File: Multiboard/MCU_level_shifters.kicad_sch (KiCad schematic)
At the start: 45 parts, among them Q1 Q_Dual_NMOS_G1S2G2D2S1D1, Q14 Q_Dual_NMOS_G1S2G2D2S1D1, Q2 Q_Dual_NMOS_G1S2G2D2S1D1, Q3 Q_Dual_NMOS_G1S2G2D2S1D1, Q4 Q_Dual_NMOS_G1S2G2D2S1D1, Q5 Q_Dual_NMOS_G1S2G2D2S1D1, Q6 Q_Dual_NMOS_G1S2G2D2S1D1, Q7 Q_Dual_NMOS_G1S2G2D2S1D1, SW3 SW_SPST, SW4 SW_SPST, SW5 SW_SPST, SW7 SW_SPST, SW9 SW_SPST

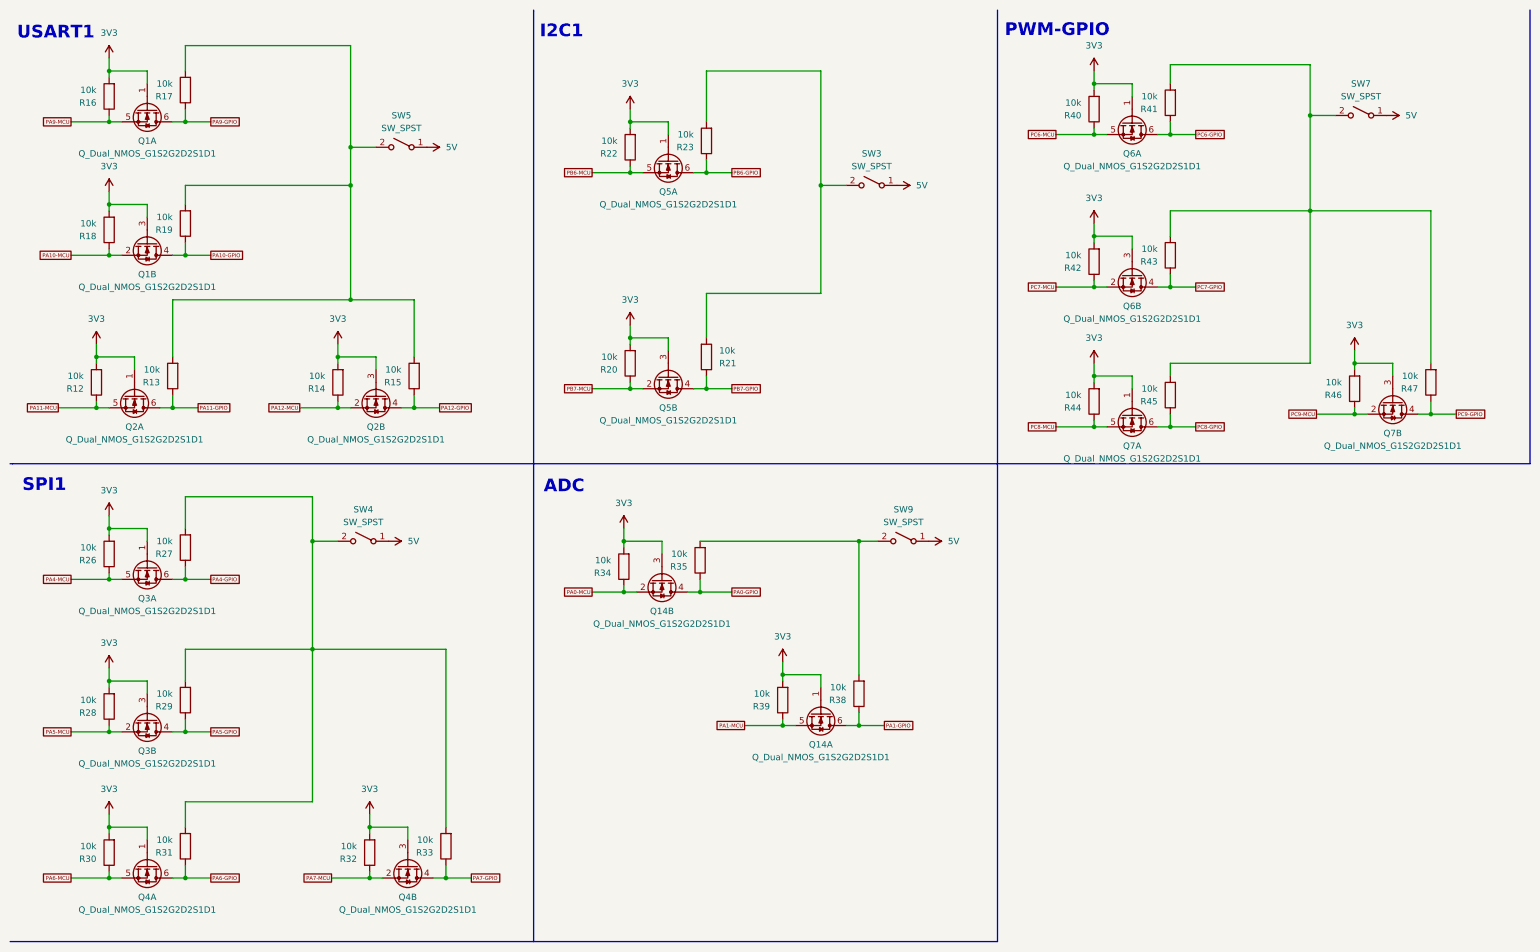
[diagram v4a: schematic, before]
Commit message: wired level shifters; positioed ldo and charge pump
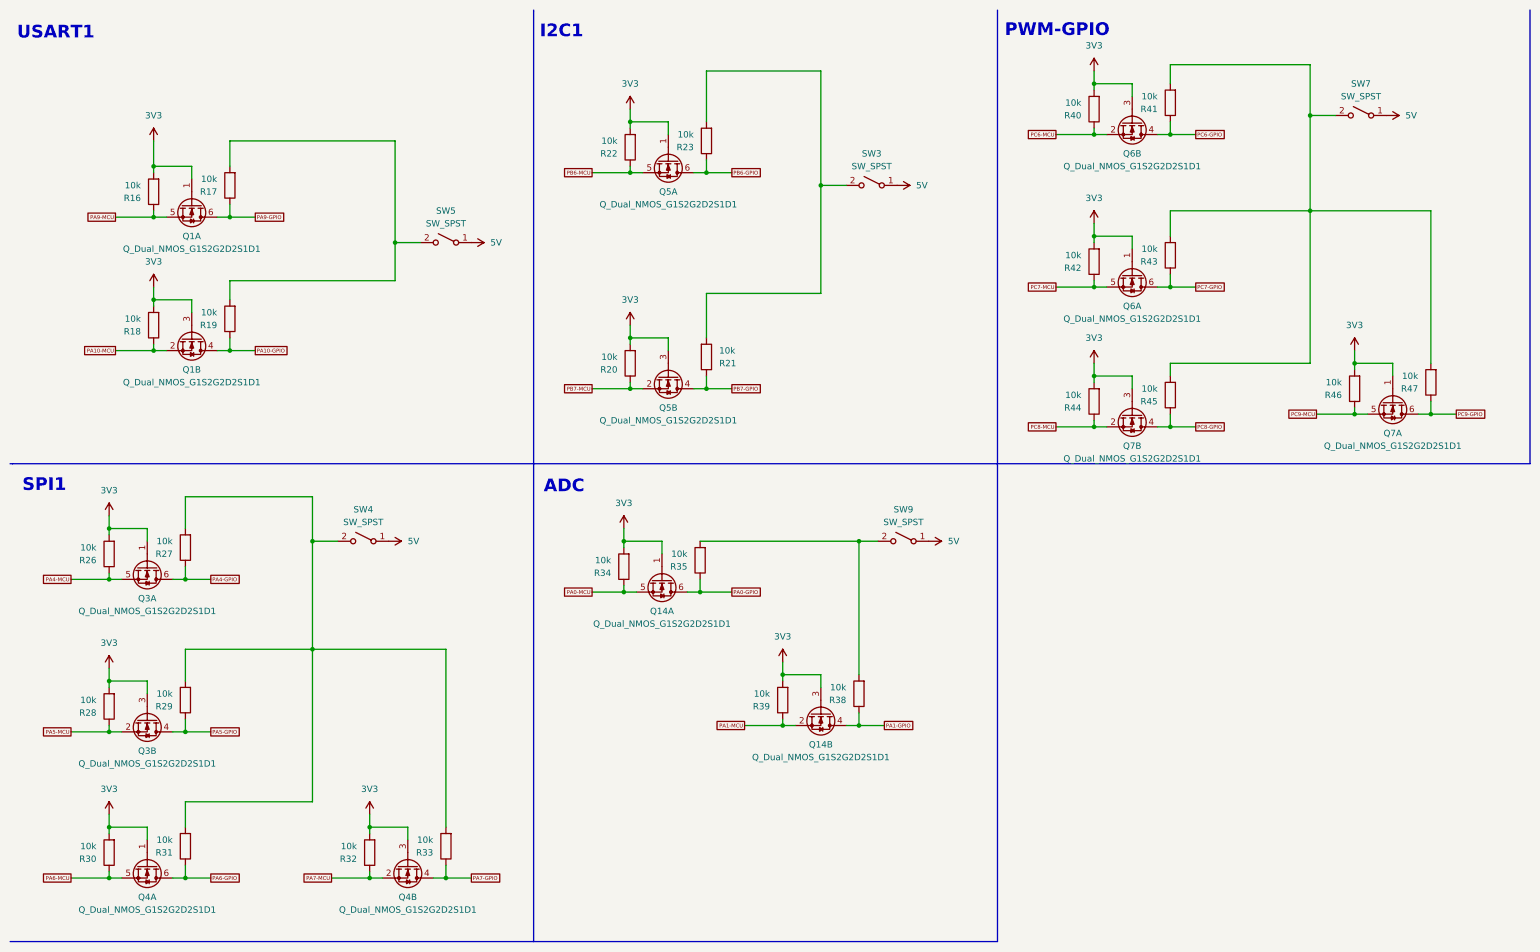
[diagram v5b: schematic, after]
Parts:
- removed Q2: Q_Dual_NMOS_G1S2G2D2S1D1, Package_TO_SOT_SMD:SOT-23-6_Handsoldering, symbol Transistor_FET:Q_Dual_NMOS_G1S2G2D2S1D1
- removed R12, R13, R14, R15: 10k, Resistor_SMD:R_0603_1608Metric_Pad0.98x0.95mm_HandSolder, symbol Device:R
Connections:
- net 3V3: now also Q14.1 (G), Q14.3 (G), Q6.1 (G), Q6.3 (G), Q7.1 (G), Q7.3 (G); no longer Q14.1 (G), Q14.3 (G), Q6.1 (G), Q6.3 (G), Q7.1 (G), Q7.3 (G)
- net PA0-GPIO: now also Q14.6 (D); no longer Q14.4 (D)
- net PA0-MCU: now also Q14.5 (S); no longer Q14.2 (S)
- net PA1-GPIO: now also Q14.4 (D); no longer Q14.6 (D)
- net PA1-MCU: now also Q14.2 (S); no longer Q14.5 (S)
- net PC6-GPIO: now also Q6.4 (D); no longer Q6.6 (D)
- net PC6-MCU: now also Q6.2 (S); no longer Q6.5 (S)
- net PC7-GPIO: now also Q6.6 (D); no longer Q6.4 (D)
- net PC7-MCU: now also Q6.5 (S); no longer Q6.2 (S)
- net PC8-GPIO: now also Q7.4 (D); no longer Q7.6 (D)
- net PC8-MCU: now also Q7.2 (S); no longer Q7.5 (S)
- net PC9-GPIO: now also Q7.6 (D); no longer Q7.4 (D)
- net PC9-MCU: now also Q7.5 (S); no longer Q7.2 (S)
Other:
- moved on the sheet: Q1A, Q1B, R16, R17, R18, R19, SW5

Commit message: Wired usb
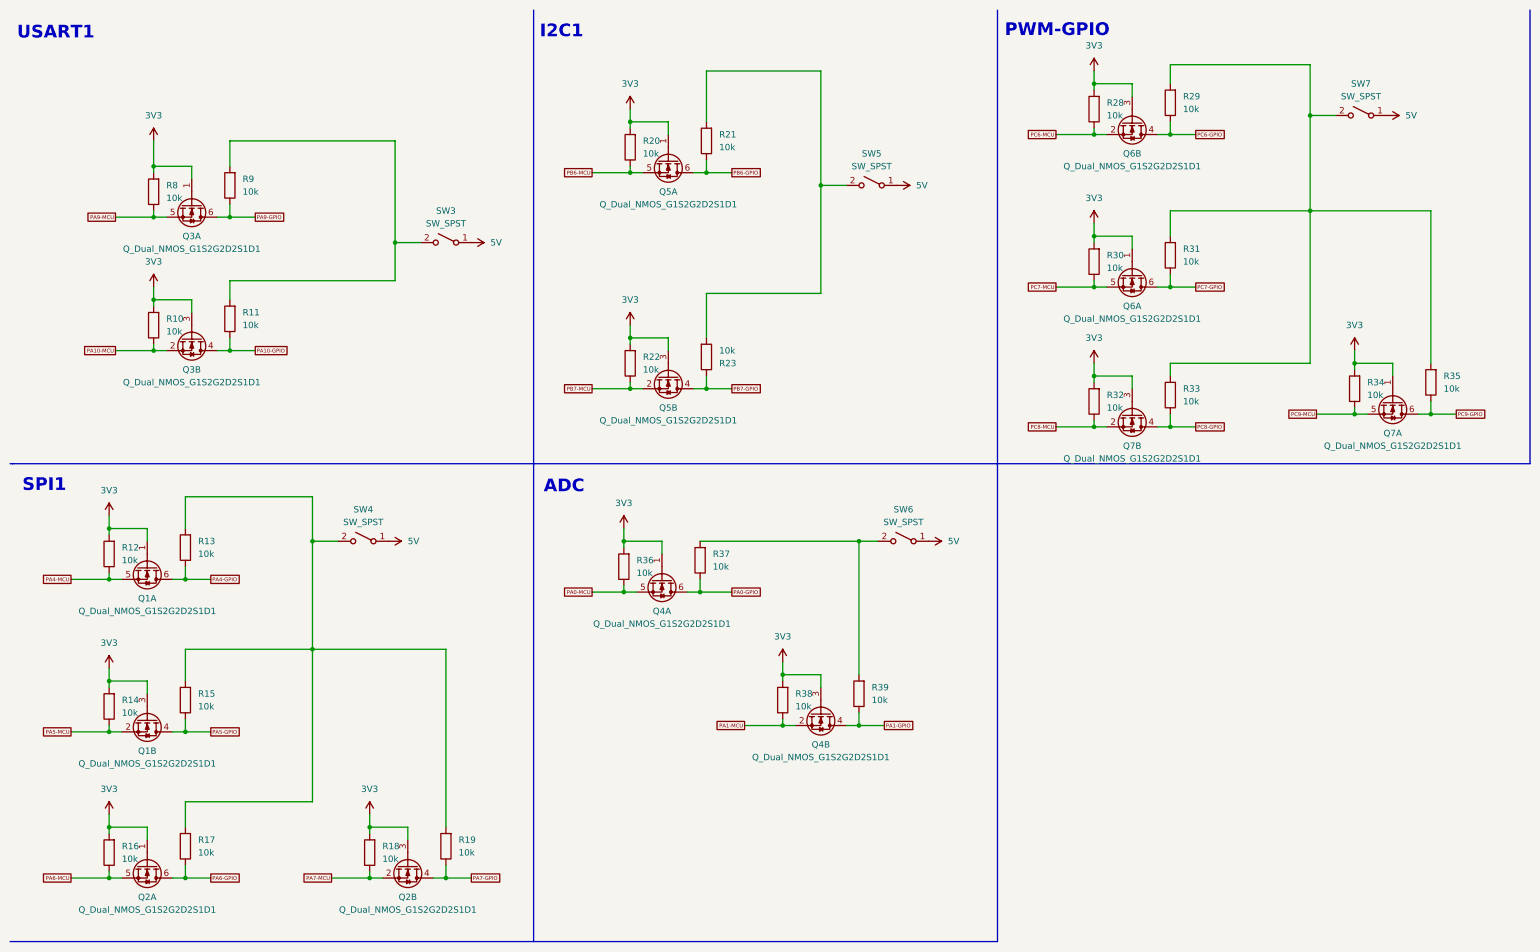
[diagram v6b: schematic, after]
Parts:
- renumbered Q3 to Q1, Q4 to Q2, Q1 to Q3, Q14 to Q4, R18 to R10, R19 to R11, R26 to R12, R27 to R13, R28 to R14, R29 to R15, R30 to R16, R31 to R17, R32 to R18, R33 to R19, R22 to R20, R23 to R21, R20 to R22, R21 to R23, R40 to R28, R41 to R29, R42 to R30, R43 to R31, R44 to R32, R45 to R33, R46 to R34, R47 to R35, R34 to R36, R35 to R37, R39 to R38, R38 to R39, R16 to R8, R17 to R9, SW5 to SW3, SW3 to SW5, SW9 to SW6

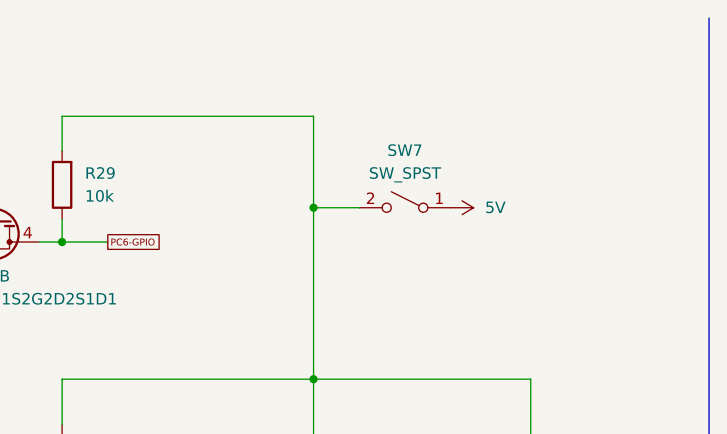
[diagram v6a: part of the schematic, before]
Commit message: Completed mcu usb-c, mcu oscillators and mcu jtag pins
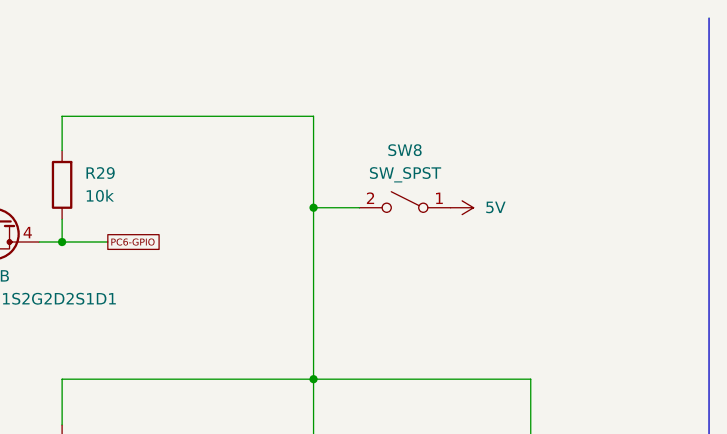
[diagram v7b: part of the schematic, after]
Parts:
- renumbered SW7 to SW8
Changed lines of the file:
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@@
 		(dnp no)
 		(fields_autoplaced yes)
-		(property "Reference" "SW7"
+		(property "Reference" "SW8"
 			(at 281.94 26.67 0)
 			(effects
@@
 			(project "Multiboard"
 				(path "/9ed4a389-3aa7-41f1-b239-280eb7f09ef1/2bca3eb5-73b3-4aa8-9f30-e1743a374253/218b9c79-34c6-4f16-af2d-c91825215b5a"
-					(reference "SW7")
+					(reference "SW8")
 					(unit 1)
 				)

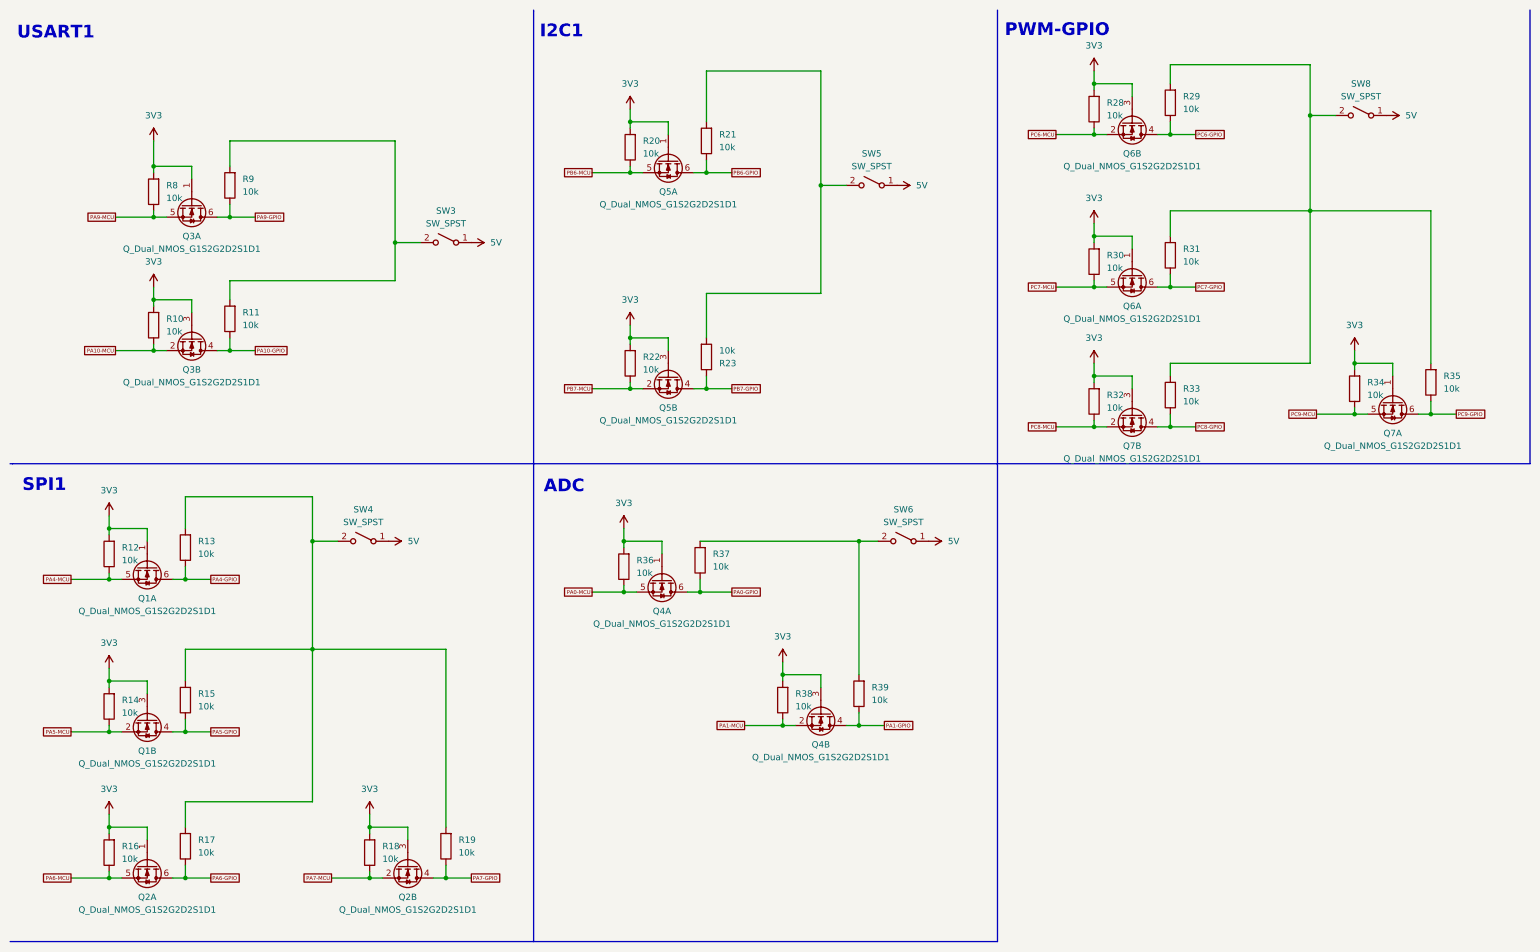
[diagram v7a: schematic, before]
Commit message: synchronised sch and pcb. Added jtag connection between fpga and ftdi
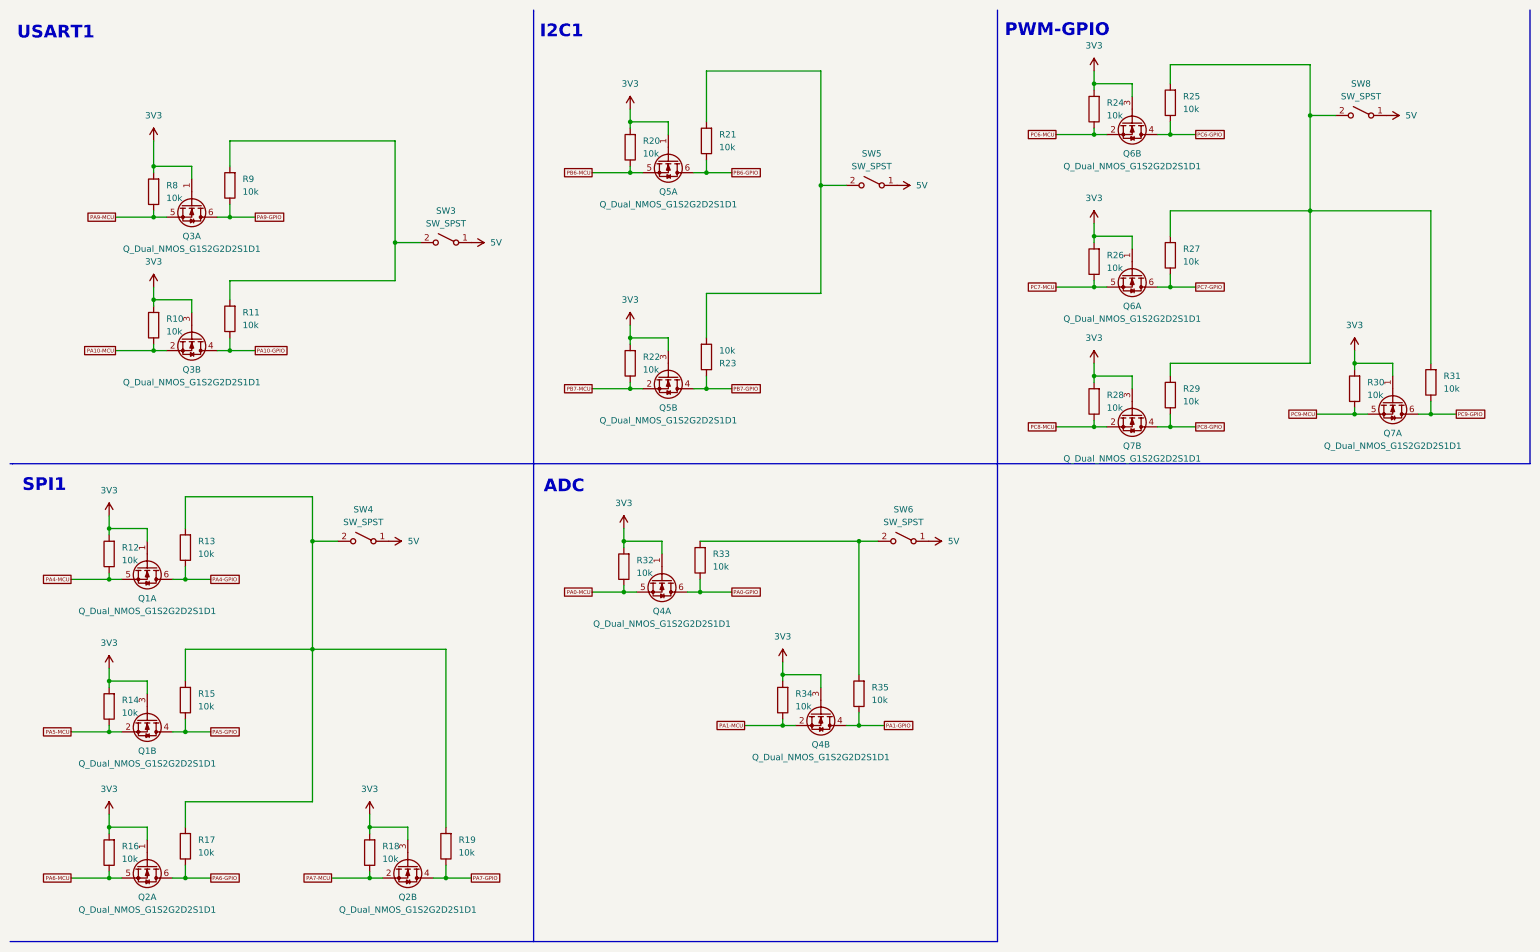
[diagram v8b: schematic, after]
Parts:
- renumbered R28 to R24, R29 to R25, R30 to R26, R31 to R27, R32 to R28, R33 to R29, R34 to R30, R35 to R31, R36 to R32, R37 to R33, R38 to R34, R39 to R35
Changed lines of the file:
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@@
 		(dnp no)
 		(fields_autoplaced yes)
-		(property "Reference" "R36"
+		(property "Reference" "R32"
 			(at 137.16 121.9199 0)
 			(effects
@@
 			(project "Multiboard"
 				(path "/9ed4a389-3aa7-41f1-b239-280eb7f09ef1/2bca3eb5-73b3-4aa8-9f30-e1743a374253/218b9c79-34c6-4f16-af2d-c91825215b5a"
-					(reference "R36")
+					(reference "R32")
 					(unit 1)
 				)
@@
 		(dnp no)
 		(fields_autoplaced yes)
-		(property "Reference" "R30"
+		(property "Reference" "R26"
 			(at 231.14 60.9599 0)
 			(effects
@@
 			(project "Multiboard"
 				(path "/9ed4a389-3aa7-41f1-b239-280eb7f09ef1/2bca3eb5-73b3-4aa8-9f30-e1743a374253/218b9c79-34c6-4f16-af2d-c91825215b5a"
-					(reference "R30")
+					(reference "R26")
 					(unit 1)
 				)
@@
 		(dnp no)
 		(fields_autoplaced yes)
-		(property "Reference" "R35"
+		(property "Reference" "R31"
 			(at 298.45 85.0899 0)
 			(effects
@@
 			(project "Multiboard"
 				(path "/9ed4a389-3aa7-41f1-b239-280eb7f09ef1/2bca3eb5-73b3-4aa8-9f30-e1743a374253/218b9c79-34c6-4f16-af2d-c91825215b5a"
-					(reference "R35")
+					(reference "R31")
 					(unit 1)
 				)
@@
 		(dnp no)
 		(fields_autoplaced yes)
-		(property "Reference" "R38"
+		(property "Reference" "R34"
 			(at 168.91 148.5899 0)
 			(effects
@@
 			(project "Multiboard"
 				(path "/9ed4a389-3aa7-41f1-b239-280eb7f09ef1/2bca3eb5-73b3-4aa8-9f30-e1743a374253/218b9c79-34c6-4f16-af2d-c91825215b5a"
-					(reference "R38")
+					(reference "R34")
 					(unit 1)
 				)
@@
 		(dnp no)
 		(fields_autoplaced yes)
-		(property "Reference" "R33"
+		(property "Reference" "R29"
 			(at 246.38 87.6299 0)
 			(effects
@@
 			(project "Multiboard"
 				(path "/9ed4a389-3aa7-41f1-b239-280eb7f09ef1/2bca3eb5-73b3-4aa8-9f30-e1743a374253/218b9c79-34c6-4f16-af2d-c91825215b5a"
-					(reference "R33")
+					(reference "R29")
 					(unit 1)
 				)
@@
 		(dnp no)
 		(fields_autoplaced yes)
-		(property "Reference" "R32"
+		(property "Reference" "R28"
 			(at 231.14 88.8999 0)
 			(effects
@@
 			(project "Multiboard"
 				(path "/9ed4a389-3aa7-41f1-b239-280eb7f09ef1/2bca3eb5-73b3-4aa8-9f30-e1743a374253/218b9c79-34c6-4f16-af2d-c91825215b5a"
-					(reference "R32")
+					(reference "R28")
 					(unit 1)
 				)
@@
 		(dnp no)
 		(fields_autoplaced yes)
-		(property "Reference" "R29"
+		(property "Reference" "R25"
 			(at 246.38 29.2099 0)
 			(effects
@@
 			(project "Multiboard"
 				(path "/9ed4a389-3aa7-41f1-b239-280eb7f09ef1/2bca3eb5-73b3-4aa8-9f30-e1743a374253/218b9c79-34c6-4f16-af2d-c91825215b5a"
-					(reference "R29")
+					(reference "R25")
 					(unit 1)
 				)
@@
 		(dnp no)
 		(fields_autoplaced yes)
-		(property "Reference" "R37"
+		(property "Reference" "R33"
 			(at 152.4 120.6499 0)
 			(effects
@@
 			(project "Multiboard"
 				(path "/9ed4a389-3aa7-41f1-b239-280eb7f09ef1/2bca3eb5-73b3-4aa8-9f30-e1743a374253/218b9c79-34c6-4f16-af2d-c91825215b5a"
-					(reference "R37")
+					(reference "R33")
 					(unit 1)
 				)
@@
 		(dnp no)
 		(fields_autoplaced yes)
-		(property "Reference" "R39"
+		(property "Reference" "R35"
 			(at 184.15 147.3199 0)
 			(effects
@@
 			(project "Multiboard"
 				(path "/9ed4a389-3aa7-41f1-b239-280eb7f09ef1/2bca3eb5-73b3-4aa8-9f30-e1743a374253/218b9c79-34c6-4f16-af2d-c91825215b5a"
-					(reference "R39")
+					(reference "R35")
 					(unit 1)
 				)
@@
 		(dnp no)
 		(fields_autoplaced yes)
-		(property "Reference" "R31"
+		(property "Reference" "R27"
 			(at 246.38 59.6899 0)
 			(effects
@@
 			(project "Multiboard"
 				(path "/9ed4a389-3aa7-41f1-b239-280eb7f09ef1/2bca3eb5-73b3-4aa8-9f30-e1743a374253/218b9c79-34c6-4f16-af2d-c91825215b5a"
-					(reference "R31")
+					(reference "R27")
 					(unit 1)
 				)
@@
 		(dnp no)
 		(fields_autoplaced yes)
-		(property "Reference" "R34"
+		(property "Reference" "R30"
 			(at 283.21 86.3599 0)
 			(effects
@@
 			(project "Multiboard"
 				(path "/9ed4a389-3aa7-41f1-b239-280eb7f09ef1/2bca3eb5-73b3-4aa8-9f30-e1743a374253/218b9c79-34c6-4f16-af2d-c91825215b5a"
-					(reference "R34")
+					(reference "R30")
 					(unit 1)
 				)
@@
 		(dnp no)
 		(fields_autoplaced yes)
-		(property "Reference" "R28"
+		(property "Reference" "R24"
 			(at 231.14 30.4799 0)
 			(effects
@@
 			(project "Multiboard"
 				(path "/9ed4a389-3aa7-41f1-b239-280eb7f09ef1/2bca3eb5-73b3-4aa8-9f30-e1743a374253/218b9c79-34c6-4f16-af2d-c91825215b5a"
-					(reference "R28")
+					(reference "R24")
 					(unit 1)
 				)
